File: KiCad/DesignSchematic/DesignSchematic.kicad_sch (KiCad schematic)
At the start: 10 parts, among them M1 Motor_DC, M2 Motor_DC, U1 EDU-CIAA, U2 AS5600, U3 AS5600, U4 MT3608, U5 VL53L0X

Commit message: Nada
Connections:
- net I2C_SDA: now reaches U2.6 (SDA)
- net I2C_SDA: now also U1.P1-19 (I2C_SDA), U3.6 (SDA), U5.4 (SDA)
- net at BT1.1 (+): now also BT2.2 (-)
- net GND: now reaches BT1.2 (-)
- net GNDDRV: now reaches M1.2 (-)
- net GNDDRV: now also M2.2 (-)
- net Vmot+: now reaches BT2.1 (+)
- net ESP_TX: now reaches U1.P2-31 (GPIO2)
- net ESP_RX: now reaches U1.P2-32 (GPIO1)
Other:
- moved on the sheet: BT1, BT2

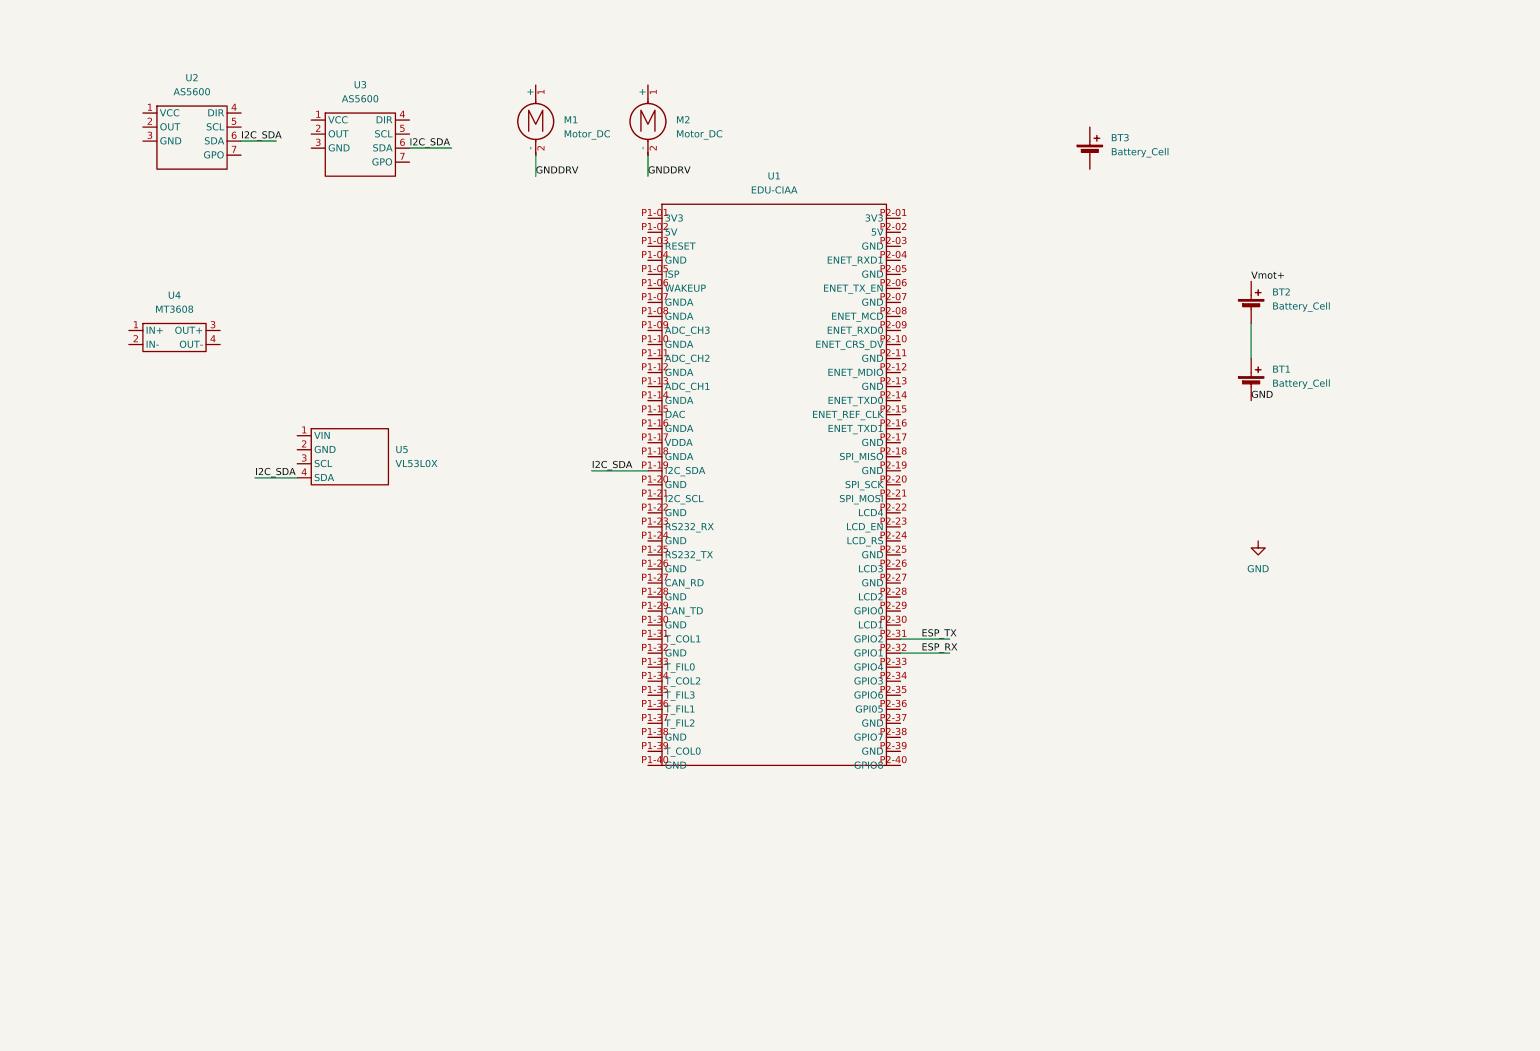
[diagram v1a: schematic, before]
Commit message: Añadido el .lck al gitignore, módulo de motores esquematizado, y añadido el esquemático del NodeMCU
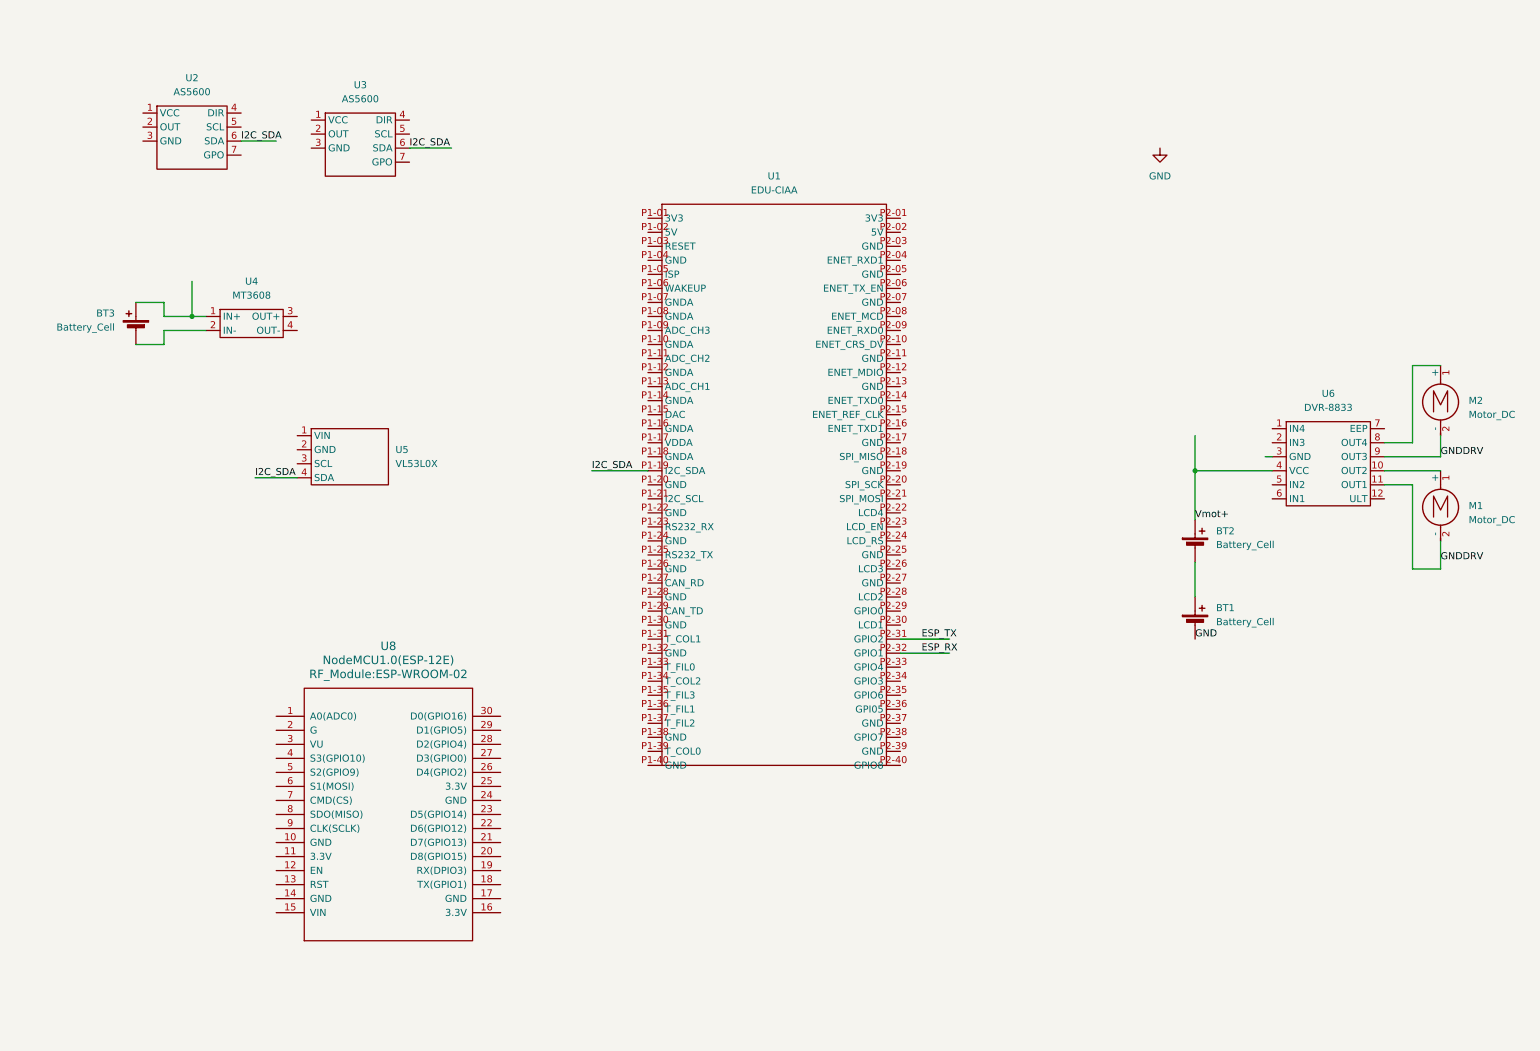
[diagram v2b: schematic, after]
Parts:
- added U6: DVR-8833, symbol Arturito:DRV8833
- added U8: NodeMCU1.0(ESP-12E), RF_Module:ESP-WROOM-02, symbol Arturito:NodeMCU1.0(ESP-12E)
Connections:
- net GNDDRV: now also U6.11 (OUT1), U6.9 (OUT3)
- net Vmot+: now also U6.4 (VCC)
- net at U4.1 (IN+): now also BT3.1 (+)
- net at U4.2 (IN-): now also BT3.2 (-)
- net at M1.1 (+): now also U6.10 (OUT2)
- net at M2.1 (+): now also U6.8 (OUT4)
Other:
- moved on the sheet: BT1, BT2, BT3, M1, M2, U4

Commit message: Editado el EDU-CIAA para que los nombres de los pines se distingan
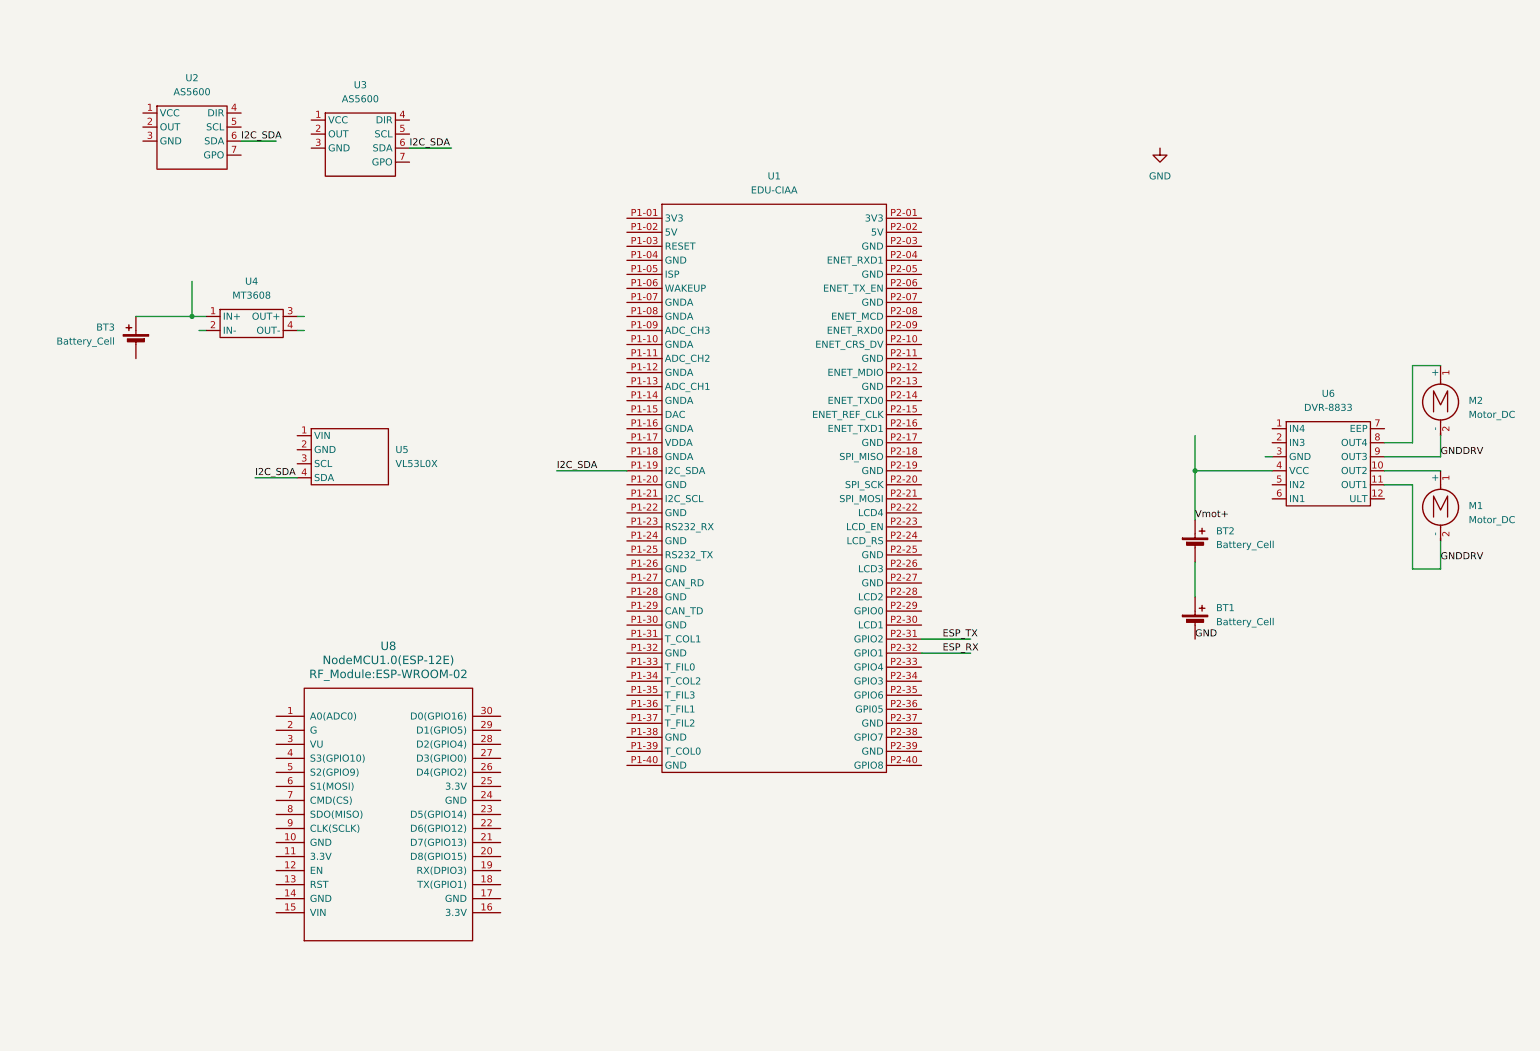
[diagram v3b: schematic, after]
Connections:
- net at U4.2 (IN-): no longer BT3.2 (-)
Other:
- moved on the sheet: BT3
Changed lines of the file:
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@@
-	(wire
-		(pts
-			(xy 38.1 67.31) (xy 43.18 67.31)
-		)
-		(stroke
-			(width 0)
-			(type default)
-		)
-	)
 	(wire
 		(pts
@@
 	(wire
 		(pts
-			(xy 38.1 72.39) (xy 38.1 69.85)
-		)
-		(stroke
-			(width 0)
-			(type default)
-		)
-	)
-	(wire
-		(pts
 			(xy 52.07 35.56) (xy 58.42 35.56)
 		)
@@
 	(wire
 		(pts
-			(xy 171.45 128.27) (xy 180.34 128.27)
-		)
-		(stroke
-			(width 0)
-			(type default)
-		)
-	)
-	(wire
-		(pts
-			(xy 38.1 64.77) (xy 33.02 64.77)
+			(xy 175.26 128.27) (xy 184.15 128.27)
+		)
+		(stroke
+			(width 0)
+			(type default)
+		)
+	)
+	(wire
+		(pts
+			(xy 33.02 67.31) (xy 43.18 67.31)
 		)
 		(stroke
@@
 	(wire
 		(pts
-			(xy 33.02 72.39) (xy 38.1 72.39)
-		)
-		(stroke
-			(width 0)
-			(type default)
-		)
-	)
-	(wire
-		(pts
 			(xy 264.16 90.17) (xy 264.16 76.2)
 		)
@@
 	(wire
 		(pts
+			(xy 44.45 69.85) (xy 45.72 69.85)
+		)
+		(stroke
+			(width 0)
+			(type default)
+		)
+	)
+	(wire
+		(pts
 			(xy 259.08 95.25) (xy 269.24 95.25)
 		)
@@
 	(wire
 		(pts
+			(xy 62.23 67.31) (xy 63.5 67.31)
+		)
+		(stroke
+			(width 0)
+			(type default)
+		)
+	)
+	(wire
+		(pts
 			(xy 259.08 92.71) (xy 269.24 92.71)
 		)
@@
 	(wire
 		(pts
-			(xy 115.57 95.25) (xy 125.73 95.25)
-		)
-		(stroke
-			(width 0)
-			(type default)
-		)
-	)
-	(wire
-		(pts
-			(xy 38.1 69.85) (xy 45.72 69.85)
+			(xy 109.22 95.25) (xy 121.92 95.25)
+		)
+		(stroke
+			(width 0)
+			(type default)
+		)
+	)
+	(wire
+		(pts
+			(xy 62.23 69.85) (xy 63.5 69.85)
 		)
 		(stroke
@@
 	(wire
 		(pts
-			(xy 38.1 67.31) (xy 38.1 64.77)
-		)
-		(stroke
-			(width 0)
-			(type default)
-		)
-	)
-	(wire
-		(pts
-			(xy 171.45 125.73) (xy 180.34 125.73)
+			(xy 175.26 125.73) (xy 184.15 125.73)
 		)
 		(stroke
@@
 	)
 	(label "I2C_SDA"
-		(at 115.57 95.25 0)
+		(at 109.22 95.25 0)
 		(effects
 			(font
@@
 	)
 	(label "ESP_TX"
-		(at 175.26 125.73 0)
+		(at 179.07 125.73 0)
 		(effects
 			(font
@@
 	)
 	(label "ESP_RX"
-		(at 175.26 128.27 0)
+		(at 179.07 128.27 0)
 		(effects
 			(font
@@
 		(length 2.54)
 		(shape round)
+		(at 33.02 74.93 180)
+		(fields_autoplaced yes)
+		(effects
+			(font
+				(size 1.27 1.27)
+				(color 0 132 0 1)
+			)
+			(justify right bottom)
+		)
+		(property "Netclass" "GND"
+			(at 33.7185 77.47 0)
+			(show_name no)
+			(do_not_autoplace no)
+			(effects
+				(font
+					(size 1.27 1.27)
+				)
+				(justify left)
+			)
+		)
+		(property "Component Class" ""
+			(at -12.7 -13.97 0)
+			(show_name no)
+			(do_not_autoplace no)
+			(effects
+				(font
+					(size 1.27 1.27)
+					(italic yes)
+				)
+			)
+		)
+	)
+	(netclass_flag ""
+		(length 2.54)
+		(shape round)
+		(at 44.45 69.85 90)
+		(effects
+			(font
+				(size 1.27 1.27)
+				(color 0 132 0 1)
+			)
+			(justify left bottom)
+		)
+		(property "Netclass" "GND"
+			(at 37.338 69.85 0)
+			(show_name no)
+			(do_not_autoplace no)
+			(effects
+				(font
+					(size 1.27 1.27)
+				)
+				(justify left)
+			)
+		)
+		(property "Component Class" ""
+			(at -7.62 -10.16 0)
+			(show_name no)
+			(do_not_autoplace no)
+			(effects
+				(font
+					(size 1.27 1.27)
+					(italic yes)
+				)
+			)
+		)
+	)
+	(netclass_flag ""
+		(length 2.54)
+		(shape round)
 		(at 237.49 92.71 90)
 		(effects
@@
 		(property "Component Class" ""
 			(at -6.35 -5.08 0)
+			(show_name no)
+			(do_not_autoplace no)
+			(effects
+				(font
+					(size 1.27 1.27)
+					(italic yes)
+				)
+			)
+		)
+	)
+	(netclass_flag ""
+		(length 2.54)
+		(shape round)
+		(at 63.5 69.85 270)
+		(effects
+			(font
+				(size 1.27 1.27)
+				(color 0 132 0 1)
+			)
+			(justify right bottom)
+		)
+		(property "Netclass" "GND"
+			(at 67.818 69.85 0)
+			(show_name no)
+			(do_not_autoplace no)
+			(effects
+				(font
+					(size 1.27 1.27)
+				)
+				(justify left)
+			)
+		)
+		(property "Component Class" ""
+			(at -10.16 -11.43 0)
+			(show_name no)
+			(do_not_autoplace no)
+			(effects
+				(font
+					(size 1.27 1.27)
+					(italic yes)
+				)
+			)
+		)
+	)
+	(netclass_flag ""
+		(length 2.54)
+		(shape round)
+		(at 63.5 67.31 270)
+		(effects
+			(font
+				(size 1.27 1.27)
+				(color 0 132 0 1)
+			)
+			(justify right bottom)
+		)
+		(property "Netclass" "6,5V"
+			(at 67.818 67.31 0)
+			(show_name no)
+			(do_not_autoplace no)
+			(effects
+				(font
+					(size 1.27 1.27)
+					(color 0 132 0 1)
+				)
+				(justify left)
+			)
+		)
+		(property "Component Class" ""
+			(at -5.08 -10.16 0)
 			(show_name no)
 			(do_not_autoplace no)
@@
 	(symbol
 		(lib_id "Device:Battery_Cell")
-		(at 33.02 69.85 0)
+		(at 33.02 72.39 0)
 		(mirror y)
 		(unit 1)
@@
 		(dnp no)
 		(property "Reference" "BT3"
-			(at 29.21 66.7384 0)
+			(at 29.21 69.2784 0)
 			(show_name no)
 			(do_not_autoplace no)
@@
 		)
 		(property "Value" "Battery_Cell"
-			(at 29.21 69.2784 0)
+			(at 29.21 71.8184 0)
 			(show_name no)
 			(do_not_autoplace no)
@@
 		)
 		(property "Footprint" ""
-			(at 33.02 68.326 90)
+			(at 33.02 70.866 90)
 			(hide yes)
 			(show_name no)
@@
 		)
 		(property "Datasheet" ""
-			(at 33.02 68.326 90)
+			(at 33.02 70.866 90)
 			(hide yes)
 			(show_name no)
@@
 		)
 		(property "Description" "Single-cell battery"
-			(at 33.02 69.85 0)
+			(at 33.02 72.39 0)
 			(hide yes)
 			(show_name no)
@@
 		)
 		(property "Sim.Device" "V"
-			(at 33.02 69.85 0)
+			(at 33.02 72.39 0)
 			(hide yes)
 			(show_name no)
@@
 		)
 		(property "Sim.Type" "DC"
-			(at 33.02 69.85 0)
+			(at 33.02 72.39 0)
 			(hide yes)
 			(show_name no)
@@
 		)
 		(property "Sim.Pins" "1=+ 2=-"
-			(at 33.02 69.85 0)
-			(hide yes)
-			(show_name no)
+			(at 33.02 72.39 0)
+			(hide yes)
+			(show_name no)

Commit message: Esquematico V1
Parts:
- added R1, R2, R3, R4: 4.7k, Package_BGA:Microchip_TFBGA-196_11x11mm_Layout14x14_P0.75mm_SMD, symbol Device:R
- added U7: MPU6050, symbol Arturito:MPU6050
- BT3: value Battery_Cell -> Battery 18650
- U8: value NodeMCU1.0(ESP-12E) -> NodeMCU3.0(ESP-12E); footprint RF_Module:ESP-WROOM-02 -> (none)
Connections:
- net Vmot+ is gone; now on net VMOT: BT2.1 (+), U6.4 (VCC)
- net ESP_RX: now also U8.19 (RX(DPIO3))
- net ESP_TX: now also U8.18 (TX(GPIO1))
- net GND: now also BT3.2 (-), U1.P4-02 (GND), U2.3 (GND), U2.4 (DIR), U3.3 (GND), U3.4 (DIR), U4.2 (IN-), U4.4 (OUT-), U5.2 (GND), U6.3 (GND), U8.14 (GND), U7.2 (GND), U7.7 (ADO)
- net +5V_SYS: now reaches U8.15 (VIN)
- net +5V_SYS: now also U1.P4-01 (5V_IN), U4.3 (OUT+)
- net EDU_3V3: now reaches U2.1 (VCC)
- net EDU_3V3: now also U1.P1-01 (3V3), U3.1 (VCC), U5.1 (VIN), R1.1, R2.1, R3.1, R4.1, U7.1 (VCC)
- net I2C1_SCL: now reaches U2.5 (SCL)
- net I2C1_SCL: now also U1.P1-23 (RS232_RX), R3.2
- net VBAT_PLACAS: now reaches BT3.1 (+), U4.1 (IN+)
- net AIN1: now reaches U6.1 (IN4)
- net AIN1: now also U1.P2-18 (SPI_MISO)
- net AIN2: now reaches U6.2 (IN3)
- net AIN2: now also U1.P2-26 (LCD3)
- net BIN1: now reaches U6.5 (IN2)
- net BIN1: now also U1.P2-28 (LCD2)
- net BIN2: now reaches U6.6 (IN1)
- net BIN2: now also U1.P2-30 (LCD1)
- net VMOT: now reaches U6.7 (EEP)
- net I2C0_SCL: now reaches U3.5 (SCL)
- net I2C0_SCL: now also U1.P1-21 (I2C_SCL), U5.3 (SCL), R2.2, U7.3 (SCL)
- net I2C1_SDA: now reaches U1.P1-25 (RS232_TX)
- net I2C1_SDA: now also U2.6 (SDA), R4.2
- net GNDDRV: no longer names the net of M1.2 (-), U6.11 (OUT1)
- net GNDDRV: no longer M2.2 (-), U6.9 (OUT3)
- net I2C_SDA renamed I2C0_SDA
- net I2C0_SDA: now also R1.2, U7.4 (SDA); no longer U2.6 (SDA)
- new net: M2.2 (-), U6.9 (OUT3)
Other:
- company: (none) -> UNLP - Facultad de Ingeniería
- title: (none) -> Arturito - Esquemático de interconexión
- moved on the sheet: BT1, BT2, BT3, M1, M2, U2, U3, U4, U5, U6, U8
